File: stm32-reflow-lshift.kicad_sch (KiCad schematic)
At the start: 16 parts, among them J6 Conn_02x08_Odd_Even, Q1 2N7002, Q10 2N7002, Q11 2N7002, Q3 2N7002, Q4 2N7002, Q5 2N7002, Q6 2N7002, Q7 2N7002, Q8 2N7002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

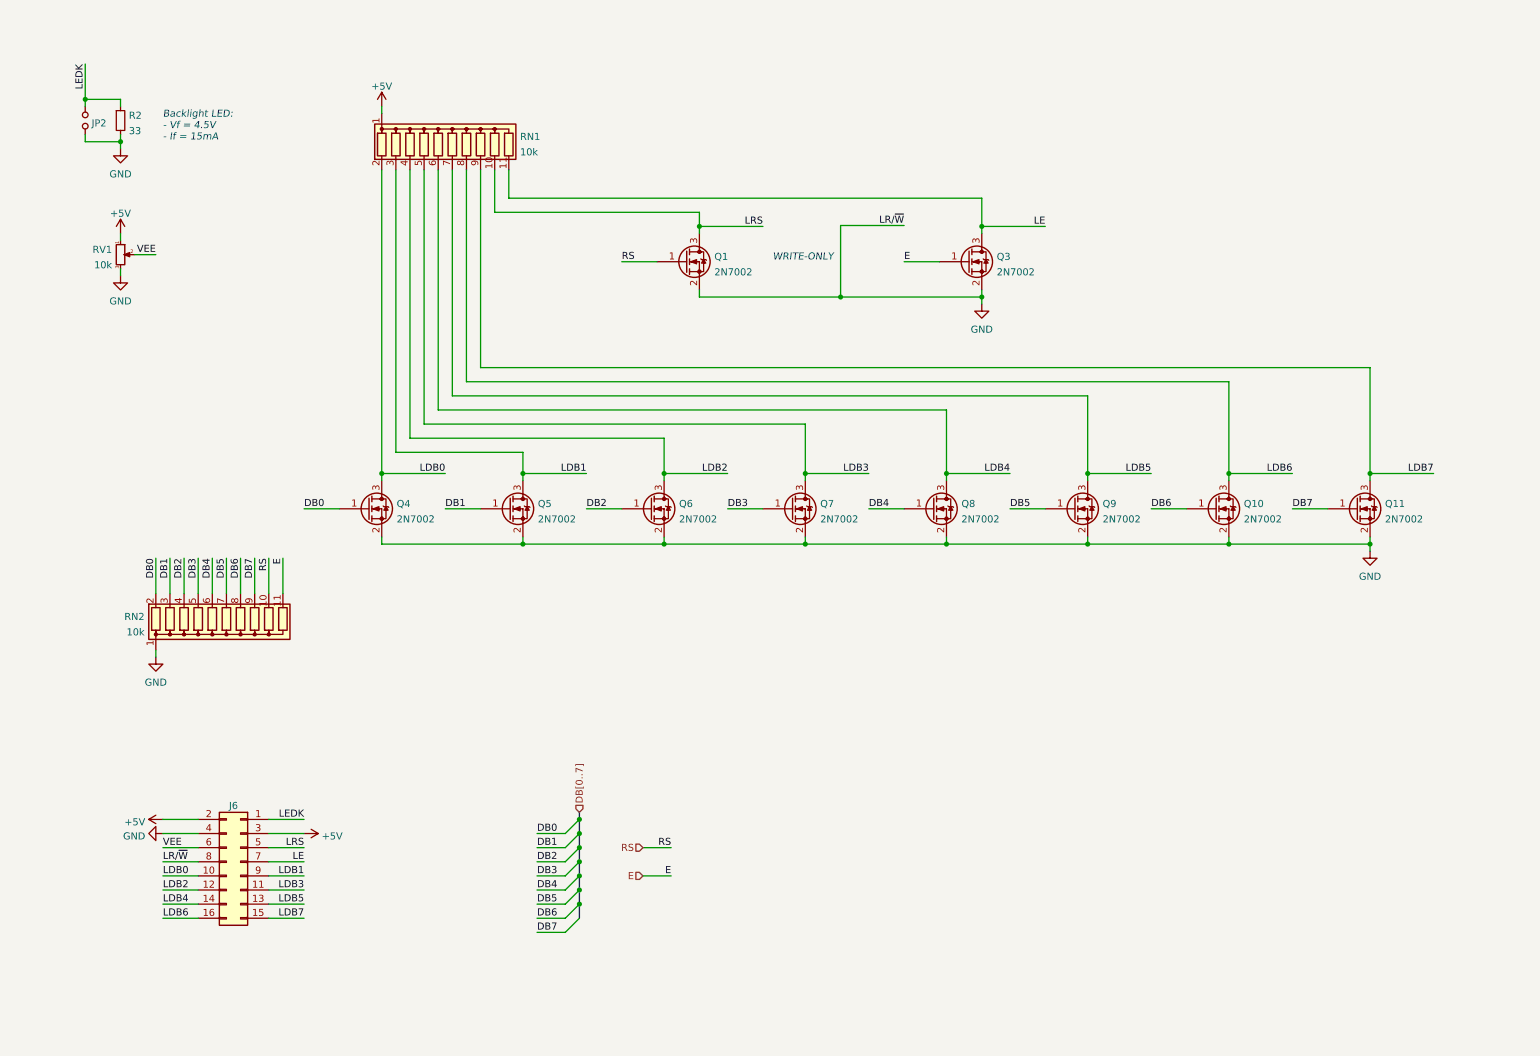
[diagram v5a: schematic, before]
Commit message: consolidated schematics for clarity, labeling and organization
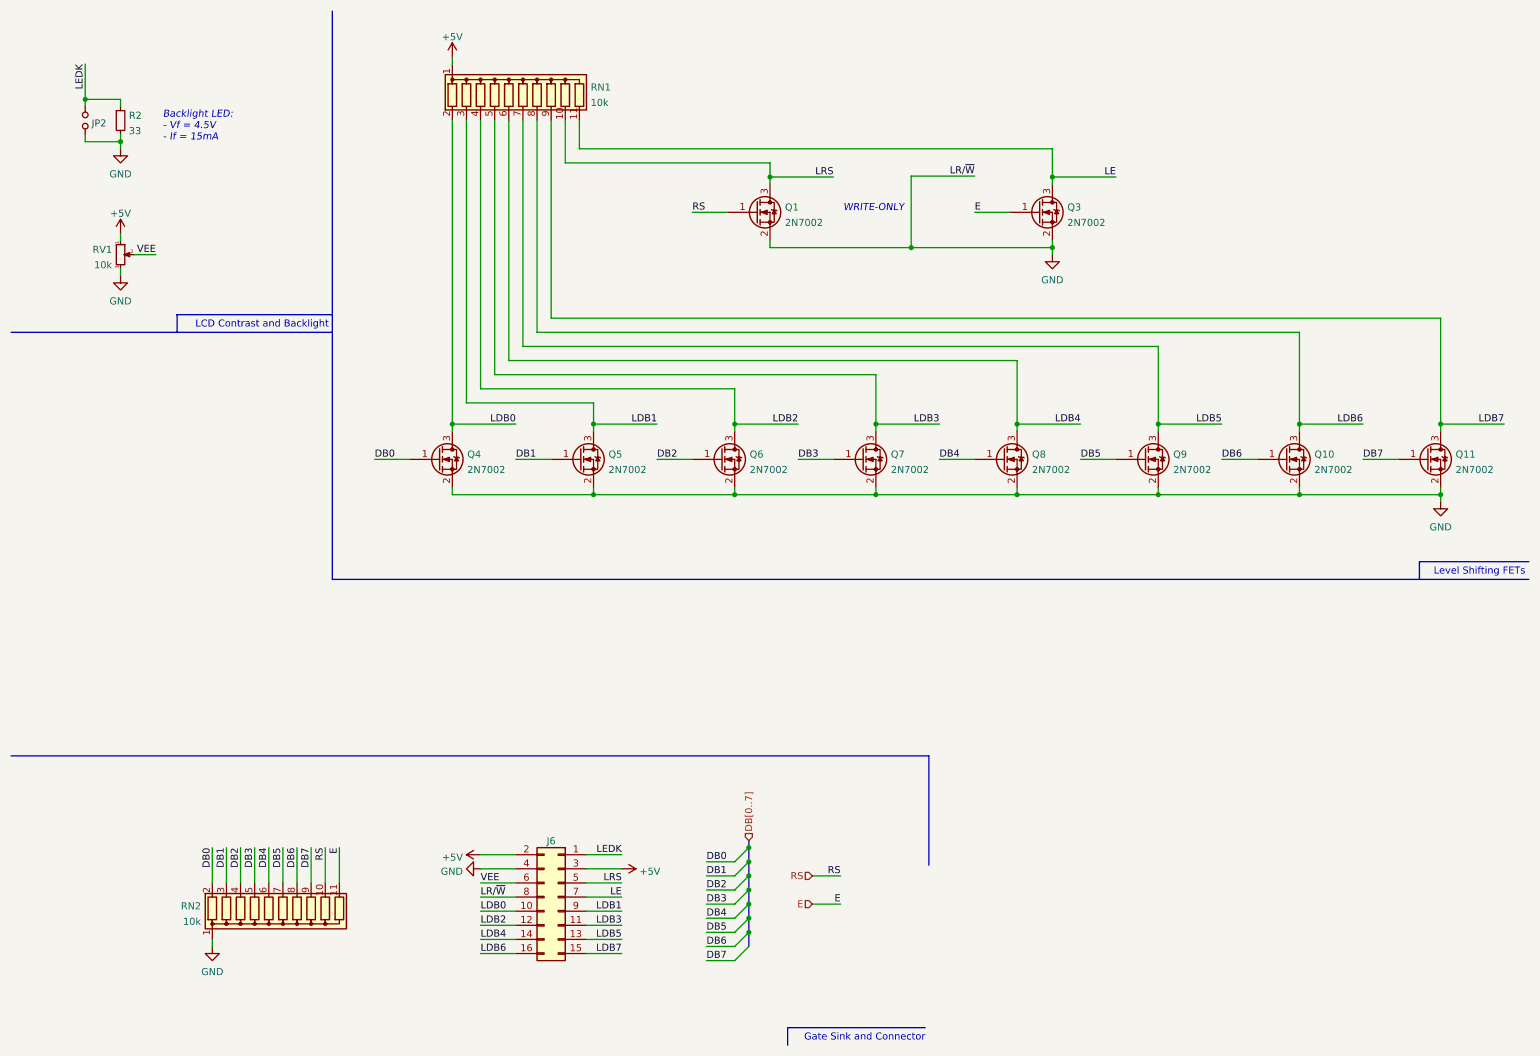
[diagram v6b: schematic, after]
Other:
- note added: "Gate Sink and Connector"
- note added: "LCD Contrast and Backlight"
- note added: "Level Shifting FETs"
- company: (none) -> de Byl Technologies, LLC
- title: (none) -> STM32 Reflow Controller
- moved on the sheet: J6, Q1, Q10, Q11, Q3, Q4, Q5, Q6, Q7, Q8, Q9, RN1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
